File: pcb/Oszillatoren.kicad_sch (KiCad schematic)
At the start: 67 parts, among them J1 Conn_01x01_Pin, J10 Conn_01x01_Pin, J11 Conn_01x01_Pin, J12 Conn_01x01_Pin, J13 Conn_01x01_Pin, J14 Conn_01x01_Pin, J15 Conn_01x01_Pin, J16 Conn_01x01_Pin, J17 Conn_01x01_Pin, J18 Conn_01x01_Pin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

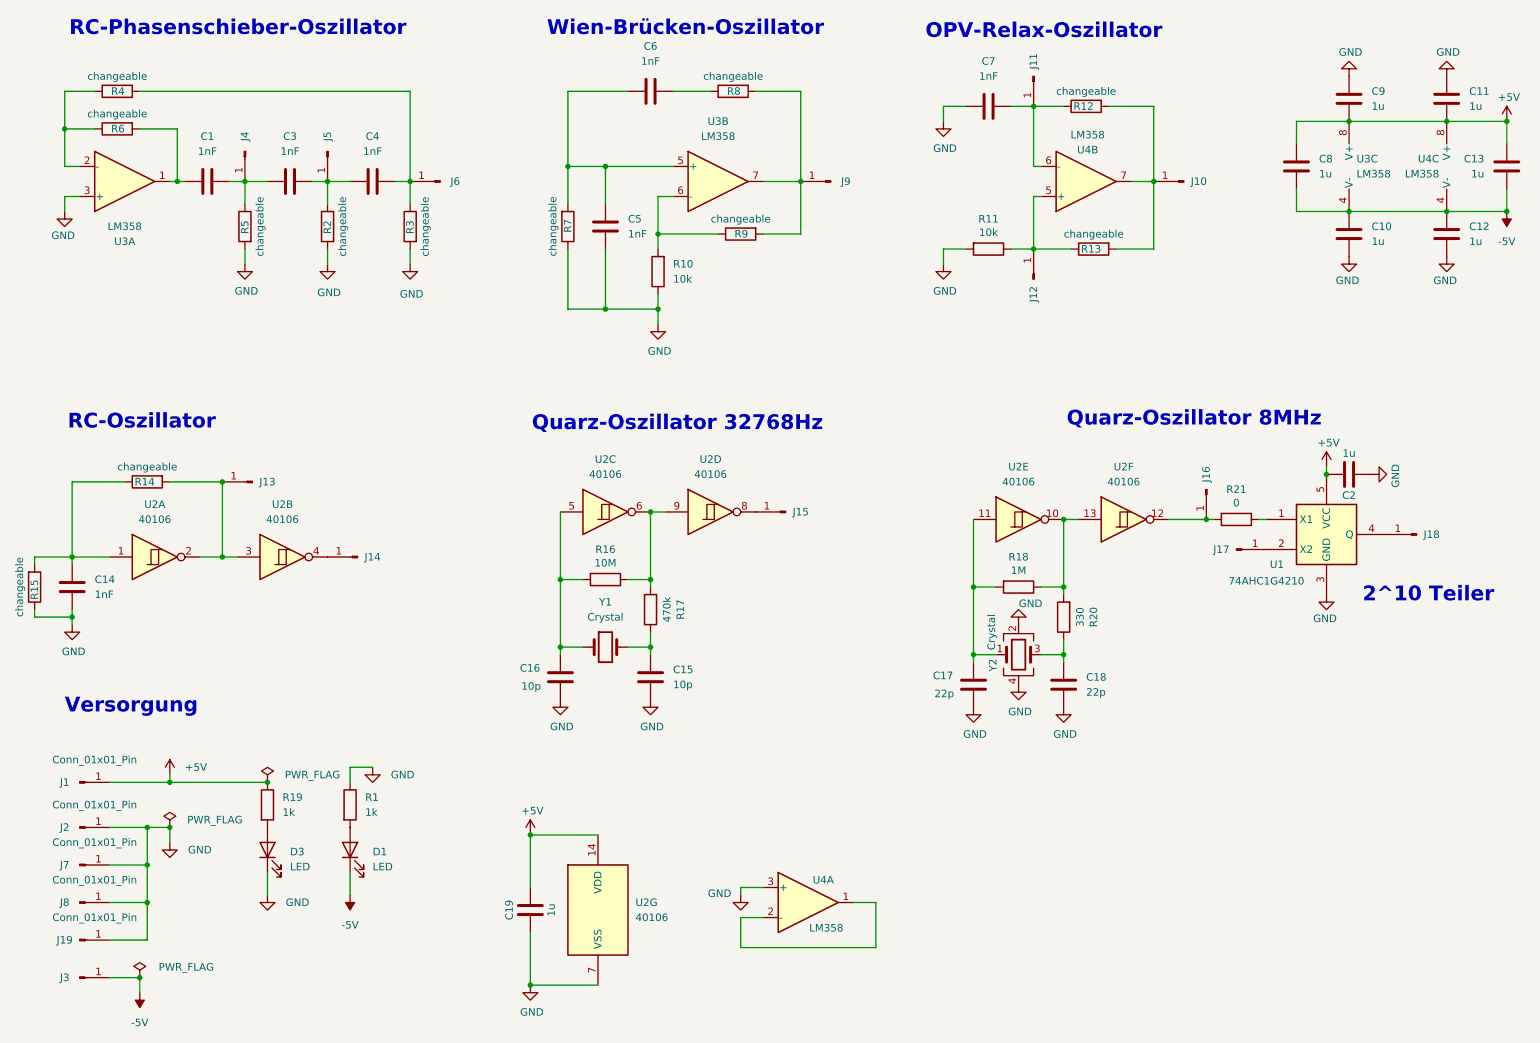
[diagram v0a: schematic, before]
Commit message: footprint-library TIH added
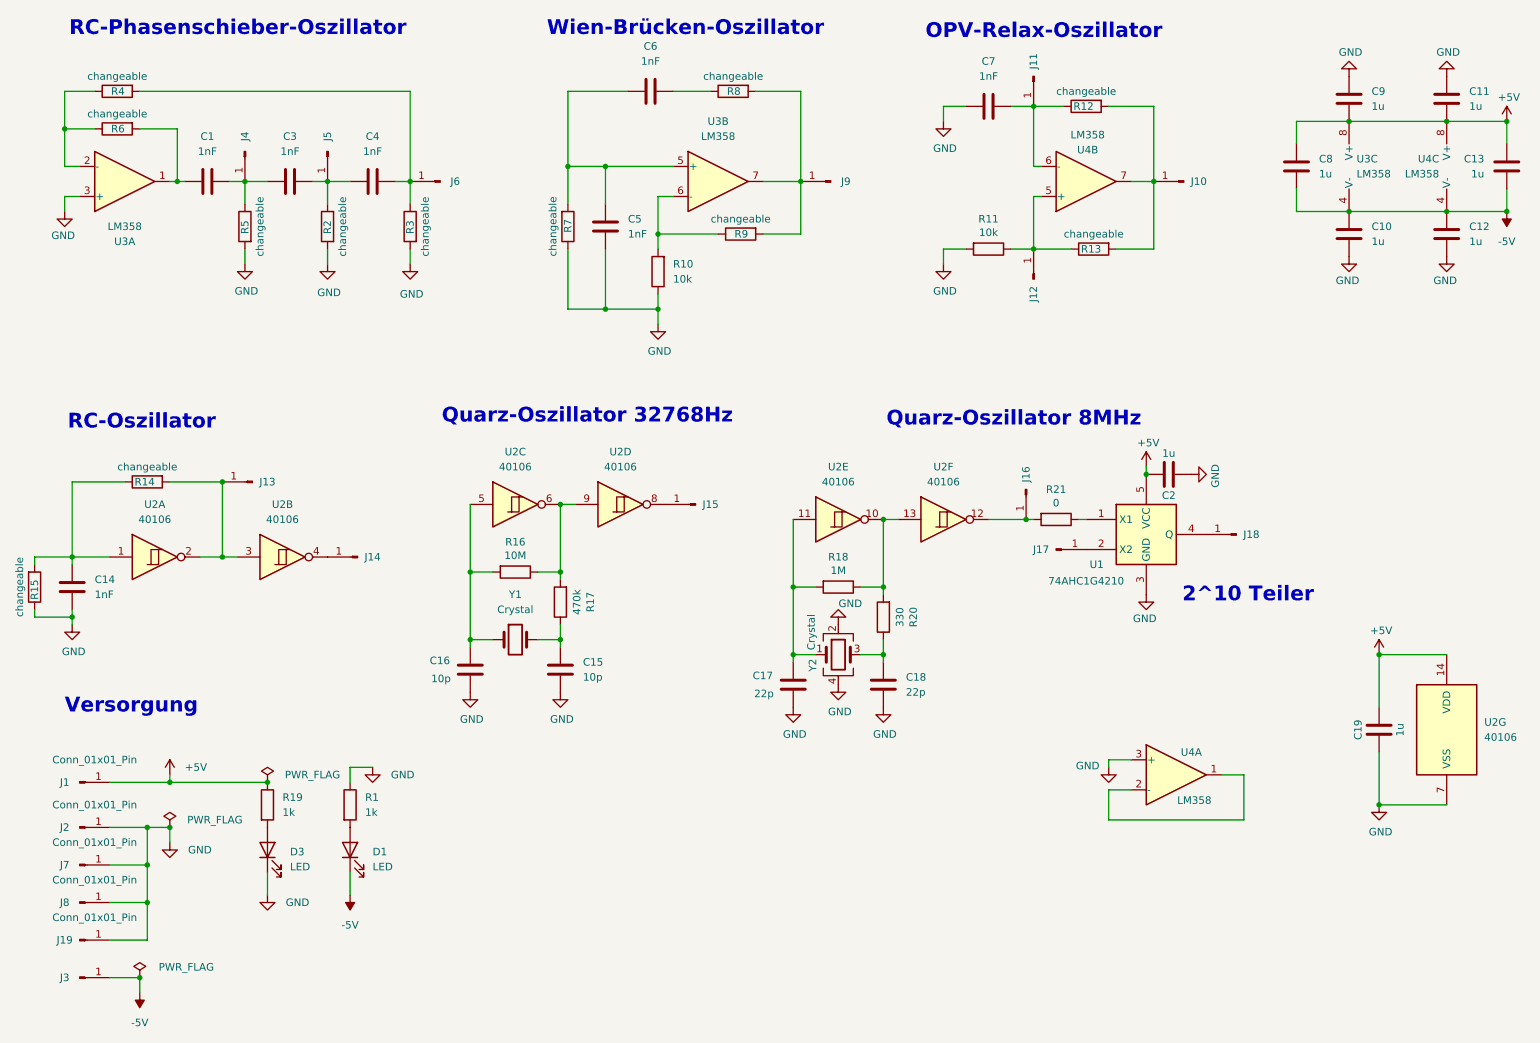
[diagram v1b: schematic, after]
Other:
- moved on the sheet: C15, C16, C17, C18, C19, C2, J15, J16, J17, J18, R16, R17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
